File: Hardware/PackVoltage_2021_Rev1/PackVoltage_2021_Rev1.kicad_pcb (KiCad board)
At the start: 2 copper layers, 203.2 x 127 mm, 139 parts, among them J3V1 Test_Point, J5V1 Test_Point, Q1 Q_NMOS_DGS, Q10 Q_NMOS_DGS, Q2 Q_NMOS_DGS, Q3 Q_NMOS_DGS, Q4 Q_NMOS_DGS, Q5 Q_NMOS_DGS, Q6 Q_NMOS_DGS, Q7 Q_NMOS_DGS, Q8 Q_NMOS_DGS, Q9 Q_NMOS_DGS, U1 LT1910, U10 INA281, U12 OKI-78SR-3.3_1.5-W36-C, U13 OKI-78SR-5_1.5-W36-C, U14 LT1910, U15 LT1910, U16 LT1910, U17 INA281, U18 INA281, U19 INA281, U2 LT1910, U20 LT1910, U21 LT1910, U22 INA281, U23 INA281, U24 TM4C129E_Launchpad, U3 LT1910, U4 INA281, U5 INA281, U6 INA281, U7 LT1910, U8 LT1910, U9 INA281

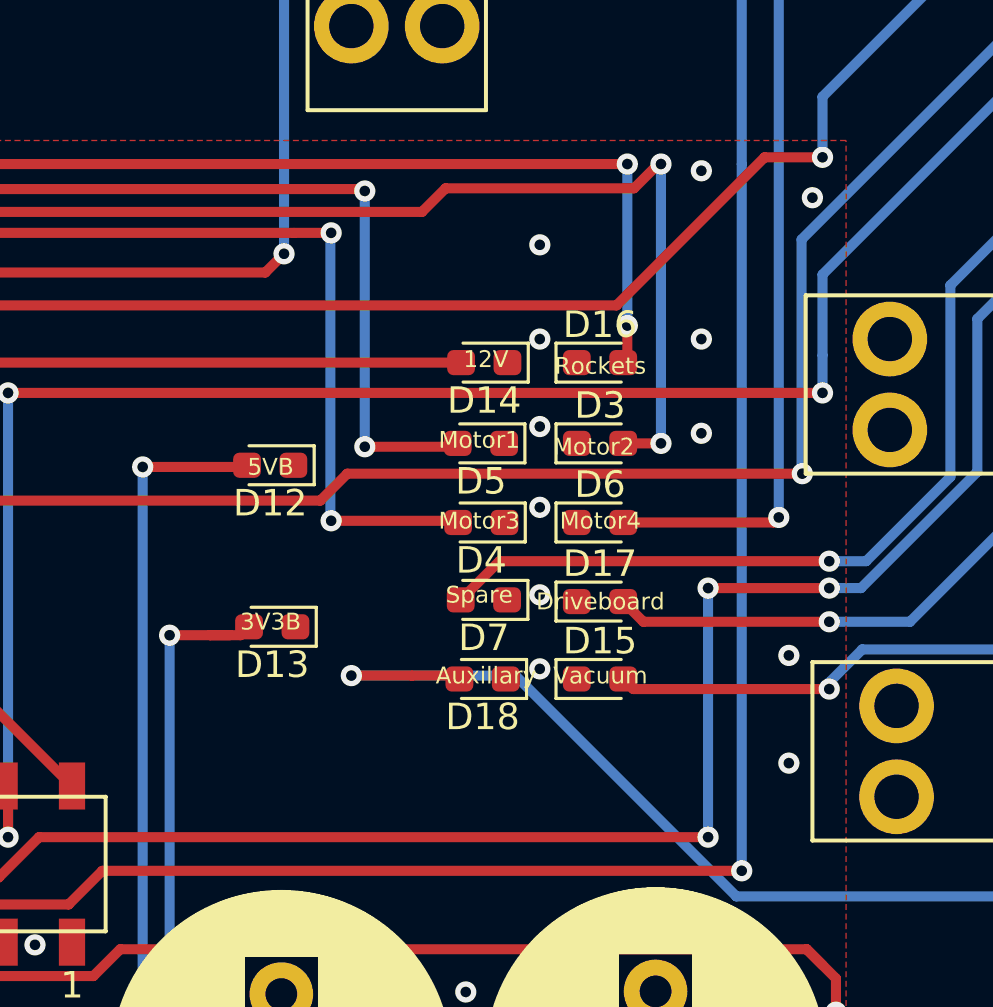
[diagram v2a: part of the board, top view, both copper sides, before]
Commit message: Moved LED labels
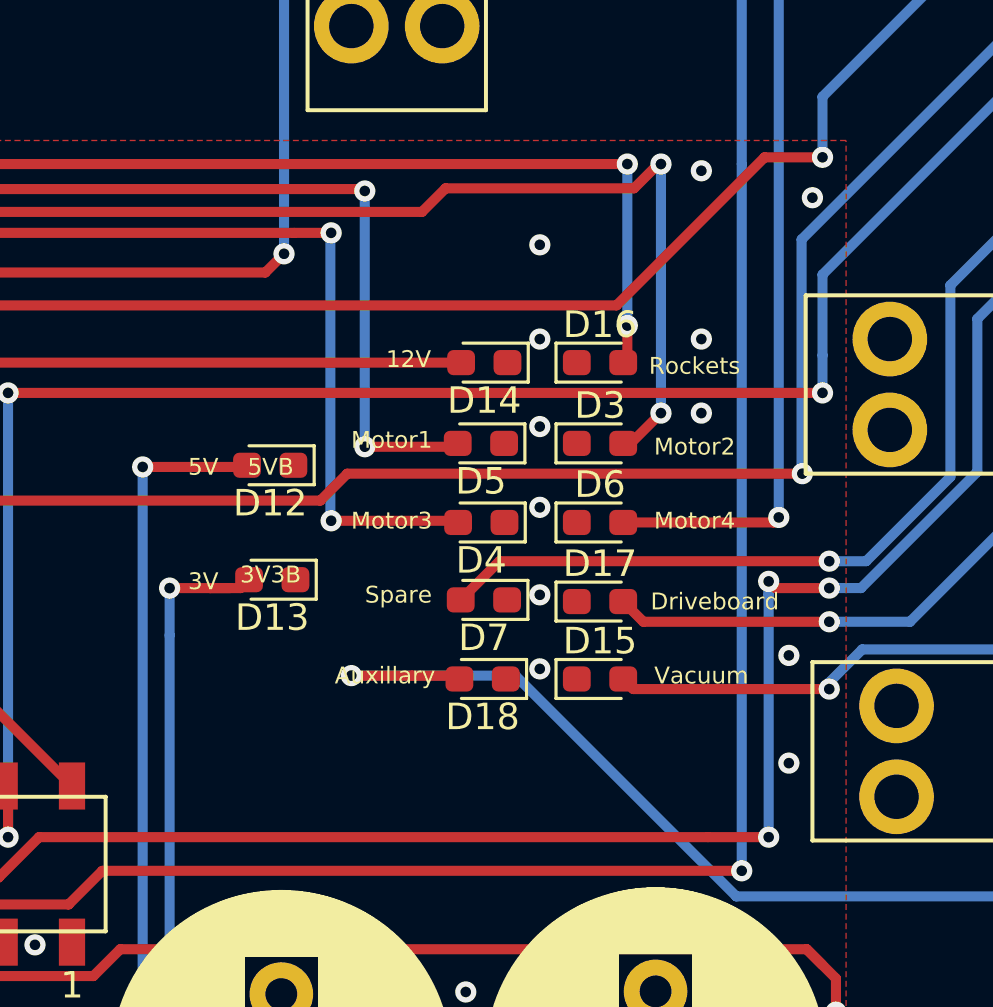
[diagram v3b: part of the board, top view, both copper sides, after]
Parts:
- moved D13 1.78 mm to (168.2, 89.6)
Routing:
- net Net-(D13-Pad2): track 79.0 -> 80.8 mm
- net Net-(D3-Pad2): track 99.1 -> 98.4 mm
- net /Current_Sensor_D1: track 85.2 -> 85.8 mm
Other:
- board text added: "3V"
- board text added: "5V"
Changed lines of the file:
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@@
   (general
     (thickness 1.6)
-    (drawings 21)
-    (tracks 1777)
+    (drawings 23)
+    (tracks 1783)
     (zones 0)
     (modules 139)
@@
   )
   (module LED_SMD:LED_0603_1608Metric_Pad1.05x0.95mm_HandSolder (layer F.Cu)
-    (at 168.2115 91.3765 180)
+    (at 168.2115 89.5985 180)
     (descr "LED SMD 0603 (1608 Metric), square (rectangular) end terminal, IPC_7351 nominal, (Body size source: http://www.tortai-tech.com/upload/download/2011102023233369053.pdf), generated with kicad-footprint-generator")
     (tags "LED handsolder")
@@
     )
   )
+  (gr_text 3V (at 165.608 89.662) (layer F.SilkS)
+    (effects (font (size 0.635 0.635) (thickness 0.15875)))
+  )
+  (gr_text 5V (at 165.608 85.344) (layer F.SilkS)
+    (effects (font (size 0.635 0.635) (thickness 0.15875)))
+  )
   (gr_arc (start 42.164 149.606) (end 38.1 149.606) (angle -90) (layer Edge.Cuts) (width 0.15))
   (gr_arc (start 42.164 30.734) (end 42.164 26.67) (angle -90) (layer Edge.Cuts) (width 0.15))
@@
     (effects (font (size 0.635 0.635) (thickness 0.15875)))
   )
-  (gr_text 3V3B (at 168.148 91.186) (layer F.SilkS)
+  (gr_text 3V3B (at 168.148 89.408) (layer F.SilkS)
     (effects (font (size 0.635 0.635) (thickness 0.15875)))
   )
-  (gr_text Auxillary (at 176.276 93.218) (layer F.SilkS)
+  (gr_text Auxillary (at 172.466 93.218) (layer F.SilkS)
     (effects (font (size 0.635 0.635) (thickness 0.15875)))
   )
-  (gr_text Driveboard (at 180.594 90.424) (layer F.SilkS)
+  (gr_text Driveboard (at 184.912 90.424) (layer F.SilkS)
     (effects (font (size 0.635 0.635) (thickness 0.15875)))
   )
-  (gr_text Vacuum (at 180.594 93.218) (layer F.SilkS)
+  (gr_text Vacuum (at 184.404 93.218) (layer F.SilkS)
     (effects (font (size 0.635 0.635) (thickness 0.15875)))
   )
-  (gr_text 12V (at 176.276 81.28) (layer F.SilkS)
+  (gr_text 12V (at 173.355 81.28) (layer F.SilkS)
     (effects (font (size 0.635 0.635) (thickness 0.15875)))
   )
-  (gr_text Rockets (at 180.594 81.534) (layer F.SilkS)
+  (gr_text Rockets (at 184.15 81.534) (layer F.SilkS)
     (effects (font (size 0.635 0.635) (thickness 0.15875)))
   )
-  (gr_text Spare (at 176.022 90.17) (layer F.SilkS)
+  (gr_text Spare (at 172.974 90.17) (layer F.SilkS)
     (effects (font (size 0.635 0.635) (thickness 0.15875)))
   )
-  (gr_text Motor4 (at 180.594 87.376) (layer F.SilkS)
+  (gr_text Motor4 (at 184.15 87.376) (layer F.SilkS)
     (effects (font (size 0.635 0.635) (thickness 0.15875)))
   )
-  (gr_text "Motor3\n" (at 176.022 87.376) (layer F.SilkS)
+  (gr_text "Motor3\n" (at 172.72 87.376) (layer F.SilkS)
     (effects (font (size 0.635 0.635) (thickness 0.15875)))
   )
-  (gr_text Motor2 (at 180.34 84.582) (layer F.SilkS)
+  (gr_text Motor2 (at 184.15 84.582) (layer F.SilkS)
     (effects (font (size 0.635 0.635) (thickness 0.15875)))
   )
-  (gr_text Motor1 (at 176.022 84.328) (layer F.SilkS)
+  (gr_text Motor1 (at 172.72 84.328) (layer F.SilkS)
     (effects (font (size 0.635 0.635) (thickness 0.15875)))
   )
@@
   (via (at 188.595 75.184) (size 0.8) (drill 0.4) (layers F.Cu B.Cu) (net 1))
   (via (at 184.404 80.518) (size 0.8) (drill 0.4) (layers F.Cu B.Cu) (net 1))
-  (via (at 184.404 84.074) (size 0.8) (drill 0.4) (layers F.Cu B.Cu) (net 1))
+  (via (at 184.404 83.312) (size 0.8) (drill 0.4) (layers F.Cu B.Cu) (net 1))
   (via (at 187.96 105.41) (size 0.8) (drill 0.4) (layers F.Cu B.Cu) (net 1))
   (via (at 186.436 107.442) (size 0.8) (drill 0.4) (layers F.Cu B.Cu) (net 1))
@@
   (segment (start 121.412 76.1585) (end 121.285 76.2855) (width 0.381) (layer B.Cu) (net 32))
   (segment (start 121.285 76.2855) (end 143.4245 76.2855) (width 0.381) (layer F.Cu) (net 32))
-  (via (at 182.88 84.455) (size 0.8) (drill 0.4) (layers F.Cu B.Cu) (net 32))
-  (segment (start 182.88 84.455) (end 181.455 84.455) (width 0.381) (layer F.Cu) (net 32) (status 20))
+  (via (at 182.88 83.312) (size 0.8) (drill 0.4) (layers F.Cu B.Cu) (net 32))
   (segment (start 143.4245 76.2855) (end 143.6785 76.2855) (width 0.381) (layer F.Cu) (net 32))
   (segment (start 143.6785 76.2855) (end 144.272 75.692) (width 0.381) (layer F.Cu) (net 32))
@@
   (segment (start 174.752 74.829942) (end 181.864 74.829942) (width 0.381) (layer F.Cu) (net 32))
   (segment (start 181.864 74.829942) (end 182.779942 73.914) (width 0.381) (layer F.Cu) (net 32))
-  (segment (start 182.88 73.914) (end 182.88 84.455) (width 0.381) (layer B.Cu) (net 32))
+  (segment (start 181.737 84.455) (end 182.88 83.312) (width 0.381) (layer F.Cu) (net 32))
+  (segment (start 181.455 84.455) (end 181.737 84.455) (width 0.381) (layer F.Cu) (net 32))
+  (segment (start 182.88 83.312) (end 182.88 73.914) (width 0.381) (layer B.Cu) (net 32))
   (via (at 154.178 59.275002) (size 0.8) (drill 0.4) (layers F.Cu B.Cu) (net 33))
   (segment (start 154.178 51.421) (end 154.178 59.275002) (width 0.381) (layer F.Cu) (net 33) (status 10))
@@
   (segment (start 189.484 131.572) (end 167.894 131.572) (width 0.381) (layer B.Cu) (net 73))
   (via (at 189.23 89.916) (size 0.8) (drill 0.4) (layers F.Cu B.Cu) (net 74))
-  (via (at 184.658 89.916) (size 0.8) (drill 0.4) (layers F.Cu B.Cu) (net 74))
-  (segment (start 189.23 89.916) (end 184.658 89.916) (width 0.381) (layer F.Cu) (net 74))
-  (via (at 184.658 99.314) (size 0.8) (drill 0.4) (layers F.Cu B.Cu) (net 74))
-  (segment (start 184.658 89.916) (end 184.658 99.314) (width 0.381) (layer B.Cu) (net 74))
+  (via (at 186.944 89.662) (size 0.8) (drill 0.4) (layers F.Cu B.Cu) (net 74))
+  (via (at 186.944 99.314) (size 0.8) (drill 0.4) (layers F.Cu B.Cu) (net 74))
   (via (at 156.972 100.838) (size 0.8) (drill 0.4) (layers F.Cu B.Cu) (net 74))
   (segment (start 157.887942 100.838) (end 156.972 100.838) (width 0.381) (layer F.Cu) (net 74))
@@
   (segment (start 201.059999 73.514001) (end 194.818 79.756) (width 0.381) (layer B.Cu) (net 74))
   (segment (start 194.818 85.52797) (end 190.42997 89.916) (width 0.381) (layer B.Cu) (net 74))
+  (segment (start 184.658 99.314) (end 186.944 99.314) (width 0.381) (layer F.Cu) (net 74))
+  (segment (start 187.198 89.916) (end 186.944 89.662) (width 0.381) (layer F.Cu) (net 74))
+  (segment (start 189.23 89.916) (end 187.198 89.916) (width 0.381) (layer F.Cu) (net 74))
+  (segment (start 186.944 90.17) (end 186.944 89.662) (width 0.381) (layer B.Cu) (net 74))
+  (segment (start 186.944 90.17) (end 186.944 99.314) (width 0.381) (layer B.Cu) (net 74))
+  (segment (start 186.944 89.916) (end 186.944 90.17) (width 0.381) (layer B.Cu) (net 74))
   (segment (start 46.9036 89.831742) (end 50.8 93.728142) (width 0.381) (layer F.Cu) (net 84))
   (segment (start 46.9036 84.154) (end 46.9036 89.831742) (width 0.381) (layer F.Cu) (net 84) (status 10))
@@
   (segment (start 131.191 136.384) (end 132.828 136.384) (width 0.381) (layer B.Cu) (net 133) (status 10))
   (segment (start 132.828 136.384) (end 132.969 136.525) (width 0.381) (layer B.Cu) (net 133))
-  (via (at 164.338 91.694) (size 0.8) (drill 0.4) (layers F.Cu B.Cu) (net 133))
-  (segment (start 167.019 91.694) (end 167.3365 91.3765) (width 0.381) (layer F.Cu) (net 133) (status 30))
-  (segment (start 165.862 91.694) (end 166.624 91.694) (width 0.381) (layer F.Cu) (net 133))
-  (segment (start 165.862 91.694) (end 167.019 91.694) (width 0.381) (layer F.Cu) (net 133) (status 20))
-  (segment (start 164.338 91.694) (end 165.862 91.694) (width 0.381) (layer F.Cu) (net 133))
+  (via (at 164.338 89.916) (size 0.8) (drill 0.4) (layers F.Cu B.Cu) (net 133))
+  (segment (start 167.019 89.916) (end 167.3365 89.5985) (width 0.381) (layer F.Cu) (net 133) (status 30))
+  (segment (start 165.862 89.916) (end 166.624 89.916) (width 0.381) (layer F.Cu) (net 133))
+  (segment (start 165.862 89.916) (end 167.019 89.916) (width 0.381) (layer F.Cu) (net 133) (status 20))
+  (segment (start 164.338 89.916) (end 165.862 89.916) (width 0.381) (layer F.Cu) (net 133))
   (segment (start 159.385 136.525) (end 164.338 131.572) (width 0.381) (layer F.Cu) (net 133))
   (segment (start 132.969 136.525) (end 159.385 136.525) (width 0.381) (layer F.Cu) (net 133))
@@
   (via (at 164.338 128.524) (size 0.8) (drill 0.4) (layers F.Cu B.Cu) (net 133))
   (segment (start 164.338 128.524) (end 164.338 91.694) (width 0.381) (layer B.Cu) (net 133))
+  (segment (start 164.338 89.916) (end 164.338 91.694) (width 0.381) (layer B.Cu) (net 133))
   (segment (start 94.488 97.5106) (end 94.615 97.3836) (width 0.381) (layer F.Cu) (net 145) (status 30))
   (zone (net 1) (net_name GND) (layer F.Cu) (hatch edge 0.508)

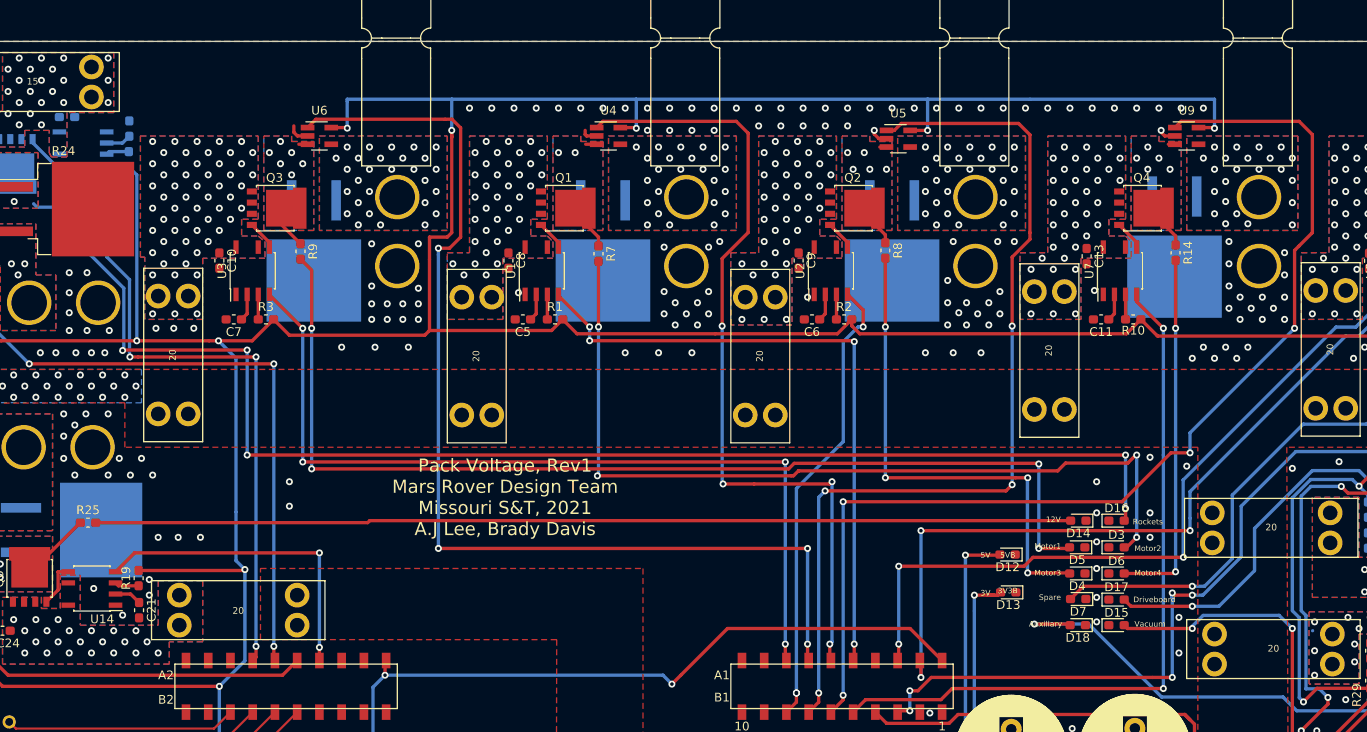
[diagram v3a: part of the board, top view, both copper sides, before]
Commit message: Moved vias, changed isolated pad of resistors to no net
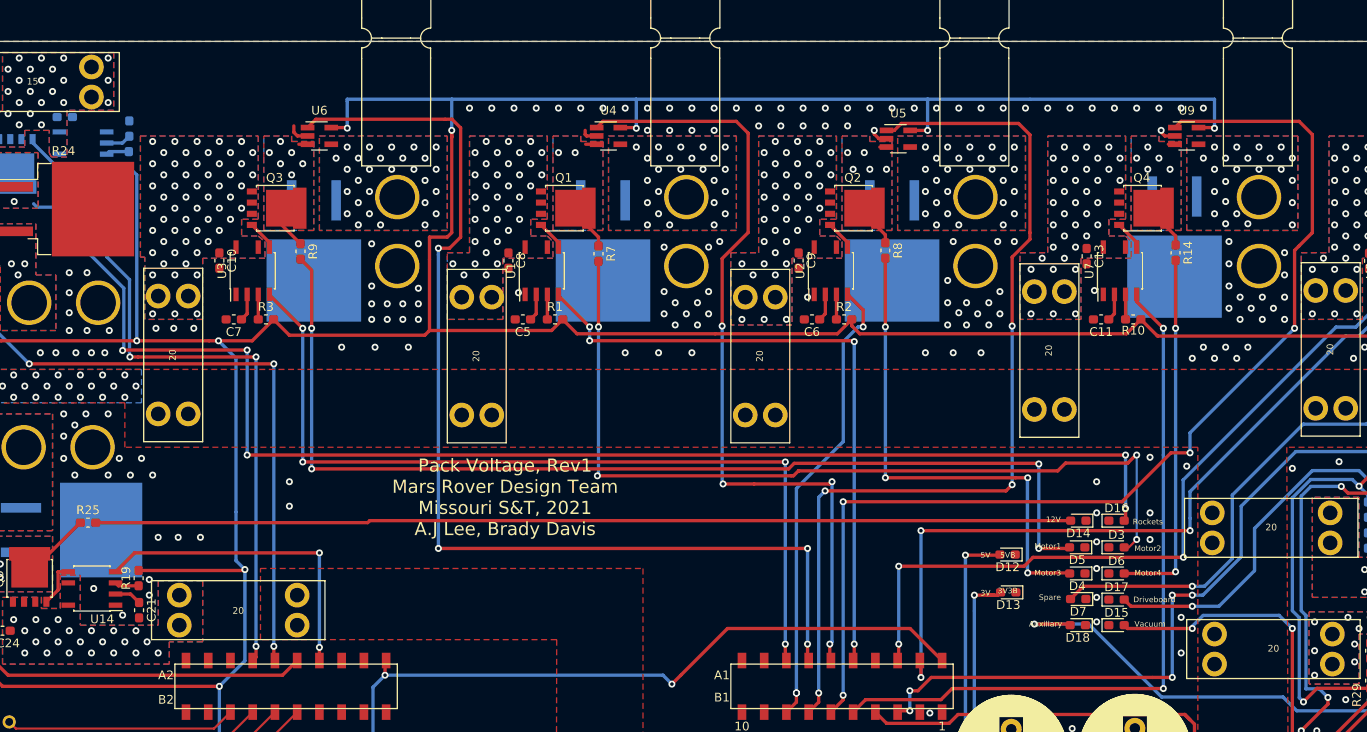
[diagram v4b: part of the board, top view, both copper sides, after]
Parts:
- moved C26 0.25 mm to (60.5, 35.3)
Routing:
- net Net-(Q8-Pad3): track 9.96 -> 2.96 mm
- net Net-(Q4-Pad3): track 9.86 -> 6.27 mm
- net Net-(Q3-Pad3): track 9.60 -> 6.01 mm
- net Net-(Q1-Pad3): track 10.5 -> 6.94 mm
- net Net-(Q2-Pad3): track 9.57 -> 5.98 mm
- net /Current_Sensor_D1: track 85.8 -> 85.2 mm

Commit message: Added signature folder and my signature to board
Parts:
- added G***: LOGO, Signature:Alee_Sig, F.Cu at (102.1, 90.2)

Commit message: Created Gerbs
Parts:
- moved G*** 6.35 mm to (108.2, 91.9)
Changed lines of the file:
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@@
       (outputformat 1)
       (mirror false)
-      (drillshape 1)
+      (drillshape 0)
       (scaleselection 1)
-      (outputdirectory ""))
+      (outputdirectory "Gerbs/"))
   )
   (net 0 "")
@@
   )
   (module Signature:Alee_Sig (layer F.Cu)
-    (at 102.108 90.17)
+    (at 108.204 91.948)
     (fp_text reference G*** (at 0 0) (layer F.SilkS) hide
       (effects (font (size 1.524 1.524) (thickness 0.3)))
@@
   (gr_arc (start 237.236 30.734) (end 241.3 30.734) (angle -90) (layer Edge.Cuts) (width 0.15))
   (gr_arc (start 237.236 149.606) (end 237.236 153.67) (angle -90) (layer Edge.Cuts) (width 0.15))
-  (gr_text "Pack Voltage, Rev1\nMars Rover Design Team\nMissouri S&T, 2021\nA.J Lee, Brady Davis\n" (at 110.744 78.74) (layer F.SilkS)
+  (gr_text "Pack Voltage, Rev1\nMars Rover Design Team\nMissouri S&T, 2021\nA.J Lee, Brady Davis\n" (at 120.904 81.788) (layer F.SilkS)
     (effects (font (size 1.5 1.5) (thickness 0.3)))
   )

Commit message: many mistakes. Need a rev2
-PV trace too small
-GND for andersons werent gnded enough
-a lot of stuff wasn't on the grid correctly
-sad
-bruh
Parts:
- moved D2 6.12 mm to (194.1, 116.3)
- moved D1 6.12 mm to (194.1, 114.0)
- moved R27 0.25 mm to (59.4, 46.5)
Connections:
- D6 pad 2: Net-(D6-Pad2) -> +5V
- R14 pad 2: Net-(D6-Pad2) -> +5V
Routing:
- net +5V: track 704.5 -> 820.6 mm, vias 15 -> 31
- net Net-(D6-Pad2): track 41.5 -> 0.00 mm, vias 2 -> 0
- net /Current_Sensor_A1: track 100.0 -> 112.8 mm
- net Net-(D15-Pad2): track 70.1 -> 78.5 mm, vias 2 -> 4
- net GND: track 21.0 -> 25.0 mm, vias 351 -> 366
- net Net-(Q5-Pad3): track 10.9 -> 13.4 mm, vias 4 -> 5
- net /Driver_R1: track 72.2 -> 70.0 mm
- net Net-(D16-Pad2): track 151.9 -> 149.9 mm
- net +3V3: track 156.5 -> 154.9 mm, vias 2 -> 5
- net Net-(D7-Pad2): track 63.6 -> 62.2 mm
- net Net-(Q4-Pad3): track 6.27 -> 5.52 mm, vias 5 -> 7
- net /Current_Sensor_V1: vias 1 -> 3
- removed copper zone on B.Cu, net Net-(C13-Pad1)
- removed copper zone on B.Cu, net Net-(C9-Pad1)
- removed copper zone on B.Cu, net Net-(Q4-Pad3)
- removed copper zone on B.Cu, net Net-(Q5-Pad3)
